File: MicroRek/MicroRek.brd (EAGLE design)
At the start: 40 x 30 mm, 41 parts, among them IC3 LSM9DS1TR

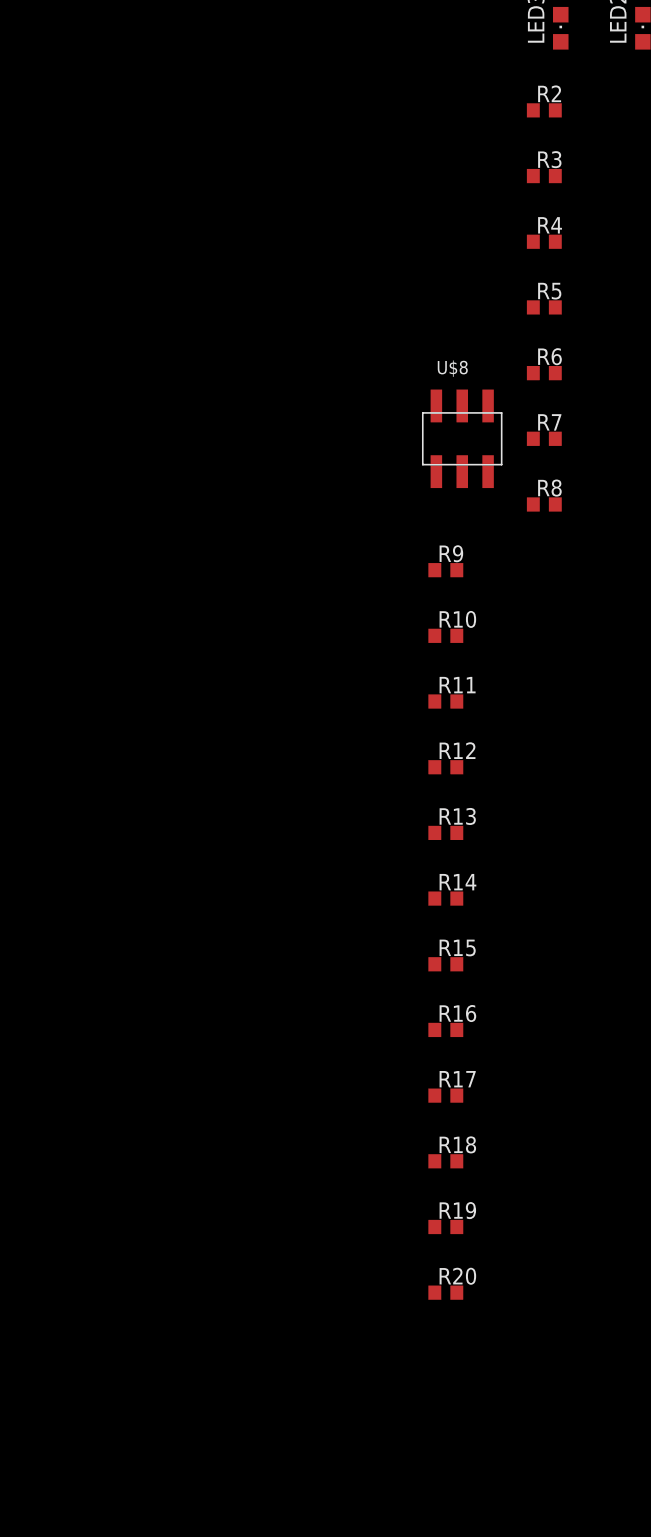
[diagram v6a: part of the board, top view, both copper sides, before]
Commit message: Added LED's
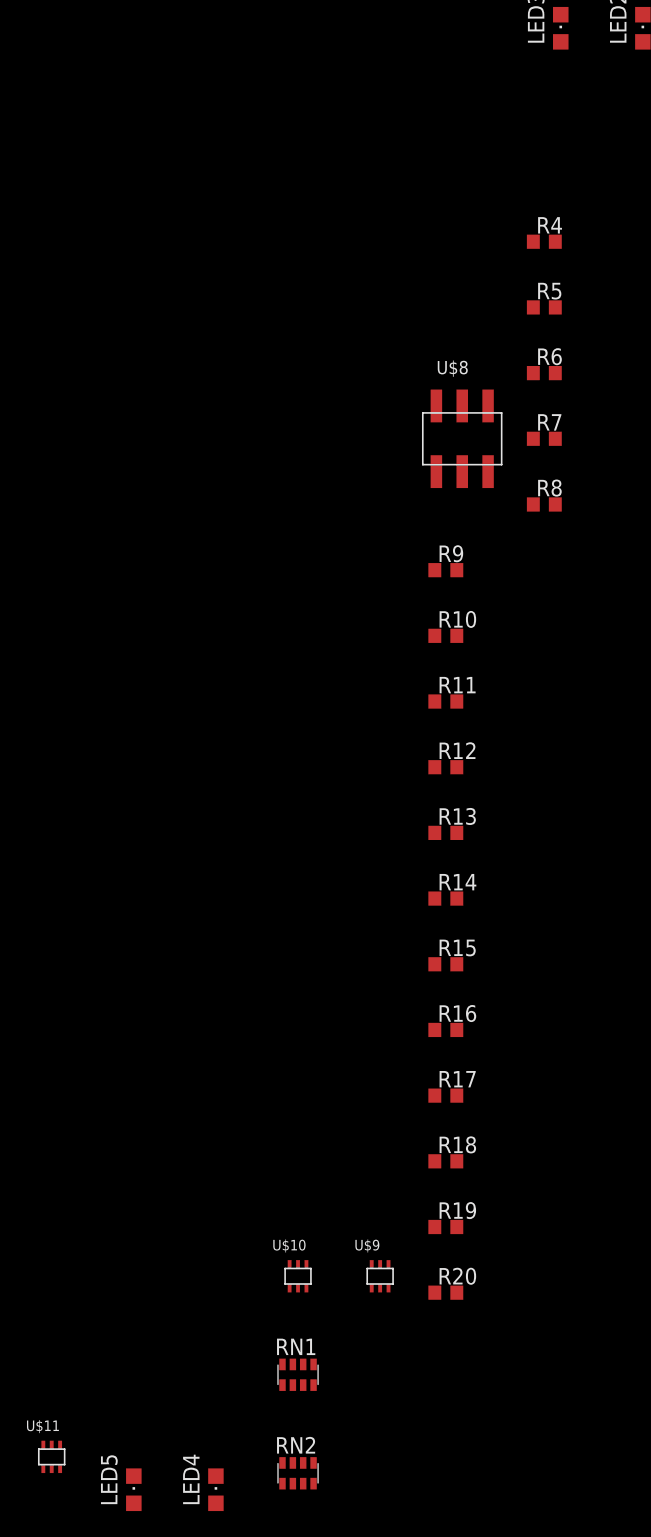
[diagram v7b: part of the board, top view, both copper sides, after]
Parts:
- removed R2: 100Ω, resistor:R0603
- removed R3: 100kΩ, resistor:R0603
- added LED4, LED5: (no value), led:CHIPLED_0805
- added RN1: CTS742C083, resistor-net:CTS742C083
- added RN2: 4.7K, resistor-net:CTS742C083
- added U$10, U$11, U$9: MBT3904DW2T1, CPSS_IC:SOT-363
- R4: value 4.7kΩ -> (none)
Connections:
- removed net N$6: LED1.C, R3.2
- new net A1: RN2.1, U$1.P20
- new net D4: RN2.2, U$1.P2
- new net D5: RN2.3, U$1.P7
- new net D6: RN2.4, U$1.P8
- new net N$10: LED5.C, RN1.4
- new net N$11: LED4.C, RN1.3
- new net N$12: LED3.C, RN1.2
- new net N$13: LED2.C, RN1.1
- new net N$14: RN2.5, U$11.P$2
- new net N$15: RN2.8, U$9.P$1
- new net N$16: RN1.7, U$11.P$4
- new net N$17: RN2.6, U$10.P$1
- new net N$18: RN1.6, U$10.P$5
- new net N$19: RN1.5, U$10.P$4
- new net N$20: RN2.7, U$10.P$2
- new net N$7: LED1.C, R4.1
- new net N$8: R4.2, U$9.P$5
- net 3.3V: now also LED2.A, LED3.A, LED4.A, LED5.A; no longer R4.1
- net 5V: now also LED1.A
- net GND: now also RN1.8, U$10.P$3, U$10.P$6, U$11.P$3, U$9.P$6; no longer R2.1, R2.2, R3.1, R4.2

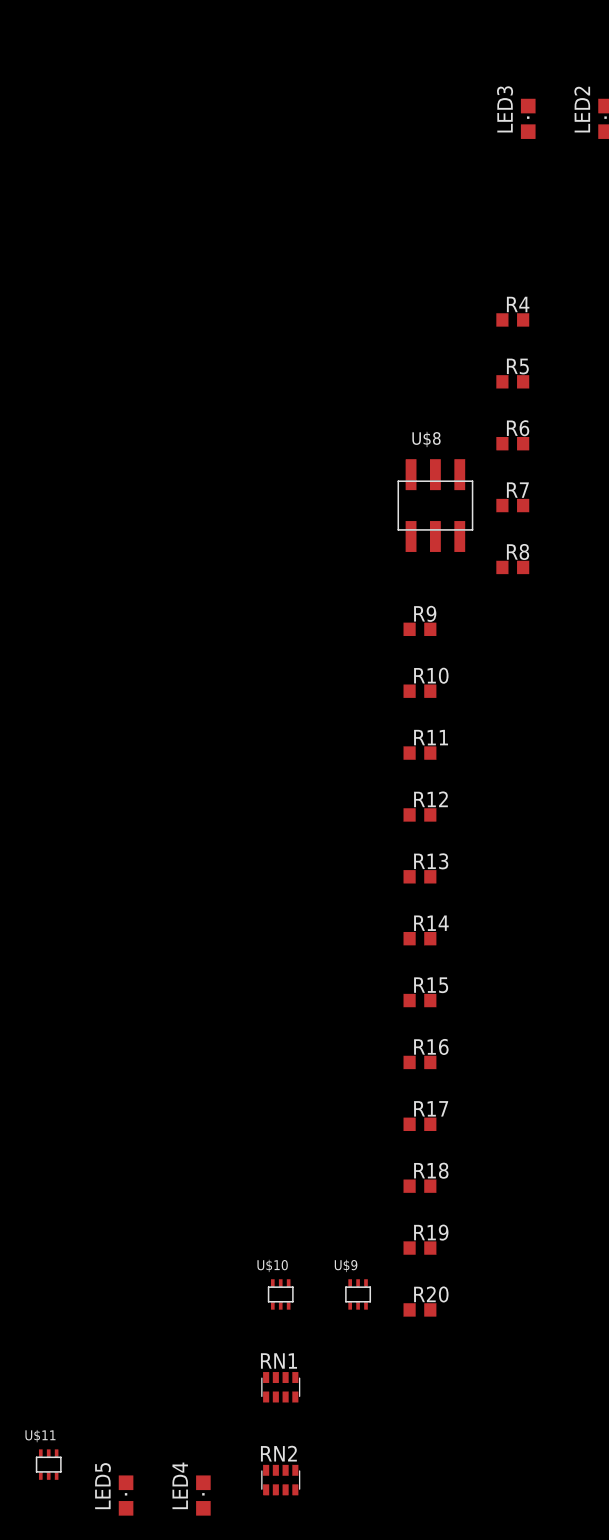
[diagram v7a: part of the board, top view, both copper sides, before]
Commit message: small led nd pullup update
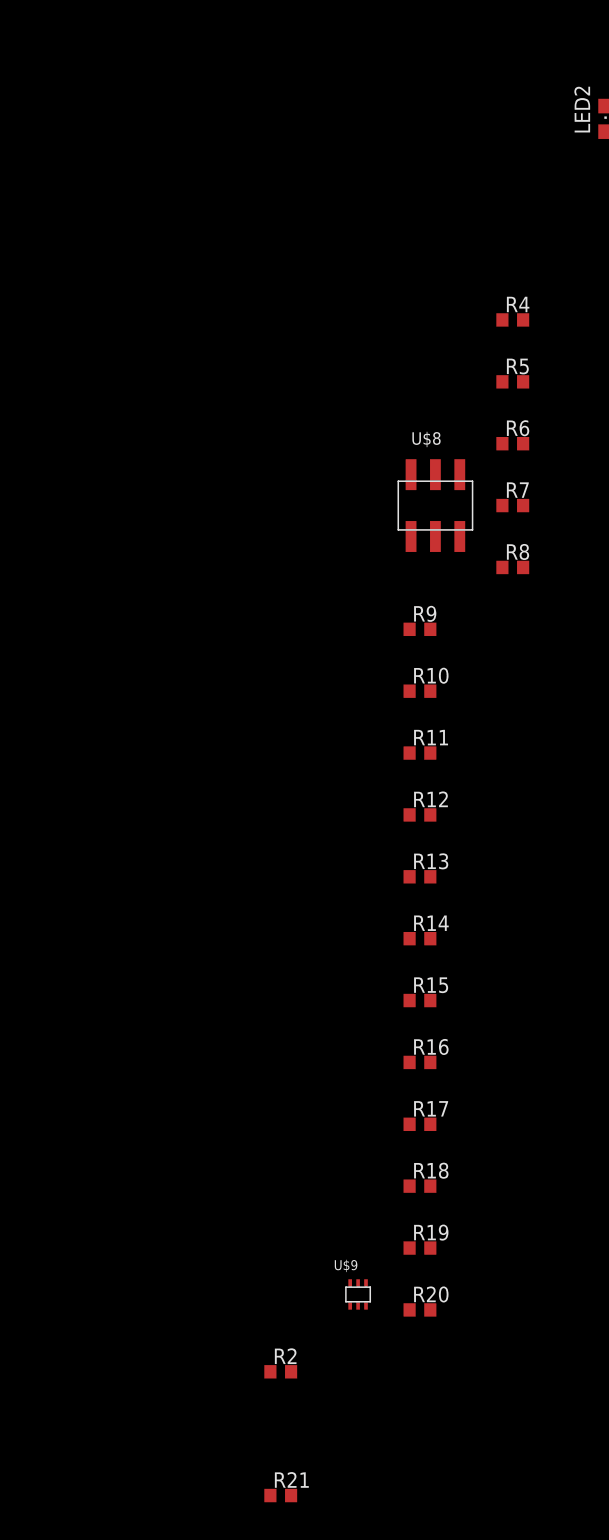
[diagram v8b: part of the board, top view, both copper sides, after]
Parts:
- removed LED3, LED4, LED5: (no value), led:CHIPLED_0805
- removed RN1: CTS742C083, resistor-net:CTS742C083
- removed RN2: 4.7K, resistor-net:CTS742C083
- removed U$10, U$11: MBT3904DW2T1, CPSS_IC:SOT-363
- added R2: 100Ω, resistor:R0603
- added R21: 4.7kΩ, resistor:R0603
- R4: value (none) -> 100KΩ
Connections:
- removed net D4: RN2.2, U$1.P2
- removed net D5: RN2.3, U$1.P7
- removed net D6: RN2.4, U$1.P8
- removed net N$10: LED5.C, RN1.4
- removed net N$11: LED4.C, RN1.3
- removed net N$13: LED2.C, RN1.1
- removed net N$14: RN2.5, U$11.P$2
- removed net N$15: RN2.8, U$9.P$1
- removed net N$16: RN1.7, U$11.P$4
- removed net N$17: RN2.6, U$10.P$1
- removed net N$18: RN1.6, U$10.P$5
- removed net N$19: RN1.5, U$10.P$4
- removed net N$20: RN2.7, U$10.P$2
- new net N$9: LED2.C, R2.1
- net 3.3V: now also R7.1, R8.1; no longer LED3.A, LED4.A, LED5.A
- net 5V: no longer R7.1, R8.1
- net A1: now also R21.1; no longer RN2.1
- net GND: now also R2.2; no longer RN1.8, U$10.P$3, U$10.P$6, U$11.P$3
- net N$12: now also R21.2, U$9.P$1; no longer LED3.C, RN1.2
